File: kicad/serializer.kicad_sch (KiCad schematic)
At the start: 8 parts, among them U501 74HC165D, U502 74HC165D, U503 74HC165D, U504 74HC165D

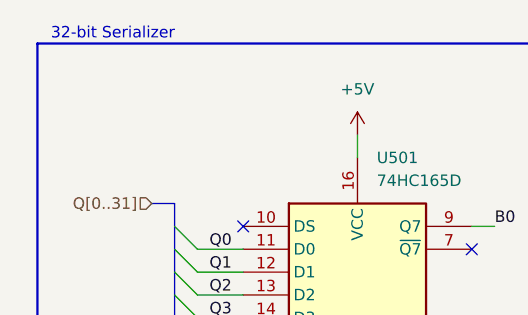
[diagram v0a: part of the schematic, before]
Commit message: rework isp header, update pinout
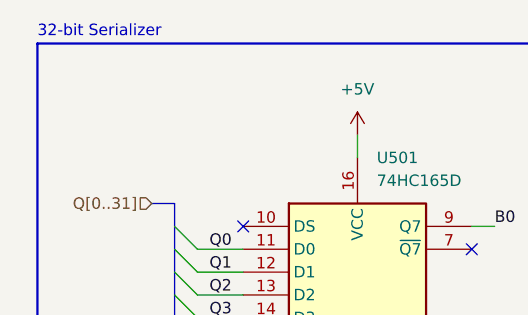
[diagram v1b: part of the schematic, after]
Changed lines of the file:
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@@
 	(title_block
 		(title "Frequency Counter")
-		(date "2025-11-19")
-		(rev "1.0")
+		(date "2025-12-25")
+		(rev "2.0-draft")
 		(company "vladaviedov.org")
 		(comment 1 "Maximum Precision (125 mHz ~ 325 MHz): 62.5 mHz")
@@
 	(text "32-bit Serializer"
 		(exclude_from_sim no)
-		(at 23.622 15.494 0)
+		(at 15.24 15.24 0)
 		(effects
 			(font
 				(size 1.27 1.27)
 			)
+			(justify left)
 		)
 	)

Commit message: replace alum caps with ceramics, change mpn labeling
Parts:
- CD501, CD502, CD503, CD504: MPN (none) -> KGM05AR51C104KH; Supplier https://www.digikey.com/en/products/detail/kyocera-avx/KGM0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 -> (none)
- U501, U502, U503, U504: MPN (none) -> 74HC165D,653; Supplier https://www.digikey.com/en/products/detail/nexperia-usa-inc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 -> (none)
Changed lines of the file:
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@@
 			)
 		)
-		(property "Supplier" "https://www.digikey.com/en/products/detail/kyocera-avx/KGM05AR51C104KH/563236"
+		(property "Supplier" ""
+			(at 66.04 66.04 0)
+			(effects
+				(font
+					(size 1.27 1.27)
+				)
+				(hide yes)
+			)
+		)
+		(property "MPN" "KGM05AR51C104KH"
 			(at 66.04 66.04 0)
 			(effects
@@
 			)
 		)
-		(property "Supplier" "https://www.digikey.com/en/products/detail/kyocera-avx/KGM05AR51C104KH/563236"
+		(property "Supplier" ""
+			(at 182.88 64.77 0)
+			(effects
+				(font
+					(size 1.27 1.27)
+				)
+				(hide yes)
+			)
+		)
+		(property "MPN" "KGM05AR51C104KH"
 			(at 182.88 64.77 0)
 			(effects
@@
 			)
 		)
-		(property "Supplier" "https://www.digikey.com/en/products/detail/kyocera-avx/KGM05AR51C104KH/563236"
+		(property "Supplier" ""
+			(at 124.46 66.04 0)
+			(effects
+				(font
+					(size 1.27 1.27)
+				)
+				(hide yes)
+			)
+		)
+		(property "MPN" "KGM05AR51C104KH"
 			(at 124.46 66.04 0)
 			(effects
@@
 			)
 		)
-		(property "Supplier" "https://www.digikey.com/en/products/detail/nexperia-usa-inc/74HC165D-653/763013"
+		(property "Supplier" ""
+			(at 50.8 52.07 0)
+			(effects
+				(font
+					(size 1.27 1.27)
+				)
+				(hide yes)
+			)
+		)
+		(property "MPN" "74HC165D,653"
 			(at 50.8 52.07 0)
 			(effects
@@
 			)
 		)
-		(property "Supplier" "https://www.digikey.com/en/products/detail/nexperia-usa-inc/74HC165D-653/763013"
+		(property "Supplier" ""
+			(at 167.64 52.07 0)
+			(effects
+				(font
+					(size 1.27 1.27)
+				)
+				(hide yes)
+			)
+		)
+		(property "MPN" "74HC165D,653"
 			(at 167.64 52.07 0)
 			(effects
@@
 			)
 		)
-		(property "Supplier" "https://www.digikey.com/en/products/detail/kyocera-avx/KGM05AR51C104KH/563236"
+		(property "Supplier" ""
+			(at 241.3 64.77 0)
+			(effects
+				(font
+					(size 1.27 1.27)
+				)
+				(hide yes)
+			)
+		)
+		(property "MPN" "KGM05AR51C104KH"
 			(at 241.3 64.77 0)
 			(effects
@@
 			)
 		)
-		(property "Supplier" "https://www.digikey.com/en/products/detail/nexperia-usa-inc/74HC165D-653/763013"
+		(property "Supplier" ""
+			(at 226.06 52.07 0)
+			(effects
+				(font
+					(size 1.27 1.27)
+				)
+				(hide yes)
+			)
+		)
+		(property "MPN" "74HC165D,653"
 			(at 226.06 52.07 0)
 			(effects
@@
 			)
 		)
-		(property "Supplier" "https://www.digikey.com/en/products/detail/nexperia-usa-inc/74HC165D-653/763013"
+		(property "Supplier" ""
 			(at 109.22 52.07 0)
 			(effects
+				(font
+					(size 1.27 1.27)
+				)
+				(hide yes)
+			)
+		)
+		(property "MPN" "74HC165D,653"
+			(at 109.22 52.07 0)
+			(effects

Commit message: assign references
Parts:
- renumbered CD501 to CD601, CD502 to CD602, CD503 to CD603, CD504 to CD604, U501 to U601, U502 to U602, U503 to U603, U504 to U604
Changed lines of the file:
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@@
 		(dnp no)
 		(fields_autoplaced yes)
-		(property "Reference" "CD501"
+		(property "Reference" "CD601"
 			(at 69.85 64.7699 0)
 			(effects
@@
 			(project ""
 				(path "/62339e8b-4e00-440f-8d81-4472a4f50c26/a3aa7686-14aa-4813-8b5a-e2293d297198"
-					(reference "CD501")
+					(reference "CD601")
 					(unit 1)
 				)
@@
 		(dnp no)
 		(fields_autoplaced yes)
-		(property "Reference" "#PWR0512"
+		(property "Reference" "#PWR0612"
 			(at 182.88 77.47 0)
 			(effects
@@
 			(project "frequency_counter"
 				(path "/62339e8b-4e00-440f-8d81-4472a4f50c26/a3aa7686-14aa-4813-8b5a-e2293d297198"
-					(reference "#PWR0512")
+					(reference "#PWR0612")
 					(unit 1)
 				)
@@
 		(dnp no)
 		(fields_autoplaced yes)
-		(property "Reference" "#PWR0515"
+		(property "Reference" "#PWR0615"
 			(at 241.3 62.23 0)
 			(effects
@@
 			(project "frequency_counter"
 				(path "/62339e8b-4e00-440f-8d81-4472a4f50c26/a3aa7686-14aa-4813-8b5a-e2293d297198"
-					(reference "#PWR0515")
+					(reference "#PWR0615")
 					(unit 1)
 				)
@@
 		(dnp no)
 		(fields_autoplaced yes)
-		(property "Reference" "CD503"
+		(property "Reference" "CD603"
 			(at 186.69 63.4999 0)
 			(effects
@@
 			(project "frequency_counter"
 				(path "/62339e8b-4e00-440f-8d81-4472a4f50c26/a3aa7686-14aa-4813-8b5a-e2293d297198"
-					(reference "CD503")
+					(reference "CD603")
 					(unit 1)
 				)
@@
 		(dnp no)
 		(fields_autoplaced yes)
-		(property "Reference" "#PWR0514"
+		(property "Reference" "#PWR0614"
 			(at 226.06 88.9 0)
 			(effects
@@
 			(project "frequency_counter"
 				(path "/62339e8b-4e00-440f-8d81-4472a4f50c26/a3aa7686-14aa-4813-8b5a-e2293d297198"
-					(reference "#PWR0514")
+					(reference "#PWR0614")
 					(unit 1)
 				)
@@
 		(dnp no)
 		(fields_autoplaced yes)
-		(property "Reference" "CD502"
+		(property "Reference" "CD602"
 			(at 128.27 64.7699 0)
 			(effects
@@
 			(project "frequency_counter"
 				(path "/62339e8b-4e00-440f-8d81-4472a4f50c26/a3aa7686-14aa-4813-8b5a-e2293d297198"
-					(reference "CD502")
+					(reference "CD602")
 					(unit 1)
 				)
@@
 		(dnp no)
 		(fields_autoplaced yes)
-		(property "Reference" "#PWR0503"
+		(property "Reference" "#PWR0603"
 			(at 66.04 63.5 0)
 			(effects
@@
 			(project "frequency_counter"
 				(path "/62339e8b-4e00-440f-8d81-4472a4f50c26/a3aa7686-14aa-4813-8b5a-e2293d297198"
-					(reference "#PWR0503")
+					(reference "#PWR0603")
 					(unit 1)
 				)
@@
 		(dnp no)
 		(fields_autoplaced yes)
-		(property "Reference" "#PWR0505"
+		(property "Reference" "#PWR0605"
 			(at 109.22 30.48 0)
 			(effects
@@
 			(project "frequency_counter"
 				(path "/62339e8b-4e00-440f-8d81-4472a4f50c26/a3aa7686-14aa-4813-8b5a-e2293d297198"
-					(reference "#PWR0505")
+					(reference "#PWR0605")
 					(unit 1)
 				)
@@
 		(dnp no)
 		(fields_autoplaced yes)
-		(property "Reference" "#PWR0502"
+		(property "Reference" "#PWR0602"
 			(at 50.8 88.9 0)
 			(effects
@@
 			(project ""
 				(path "/62339e8b-4e00-440f-8d81-4472a4f50c26/a3aa7686-14aa-4813-8b5a-e2293d297198"
-					(reference "#PWR0502")
+					(reference "#PWR0602")
 					(unit 1)
 				)
@@
 		(dnp no)
 		(fields_autoplaced yes)
-		(property "Reference" "#PWR0504"
+		(property "Reference" "#PWR0604"
 			(at 66.04 78.74 0)
 			(effects
@@
 			(project "frequency_counter"
 				(path "/62339e8b-4e00-440f-8d81-4472a4f50c26/a3aa7686-14aa-4813-8b5a-e2293d297198"
-					(reference "#PWR0504")
+					(reference "#PWR0604")
 					(unit 1)
 				)
@@
 		(dnp no)
 		(fields_autoplaced yes)
-		(property "Reference" "#PWR0513"
+		(property "Reference" "#PWR0613"
 			(at 226.06 30.48 0)
 			(effects
@@
 			(project "frequency_counter"
 				(path "/62339e8b-4e00-440f-8d81-4472a4f50c26/a3aa7686-14aa-4813-8b5a-e2293d297198"
-					(reference "#PWR0513")
+					(reference "#PWR0613")
 					(unit 1)
 				)
@@
 		(dnp no)
 		(fields_autoplaced yes)
-		(property "Reference" "U501"
+		(property "Reference" "U601"
 			(at 52.9433 29.21 0)
 			(effects
@@
 			(project "frequency_counter"
 				(path "/62339e8b-4e00-440f-8d81-4472a4f50c26/a3aa7686-14aa-4813-8b5a-e2293d297198"
-					(reference "U501")
+					(reference "U601")
 					(unit 1)
 				)
@@
 		(dnp no)
 		(fields_autoplaced yes)
-		(property "Reference" "#PWR0508"
+		(property "Reference" "#PWR0608"
 			(at 124.46 78.74 0)
 			(effects
@@
 			(project "frequency_counter"
 				(path "/62339e8b-4e00-440f-8d81-4472a4f50c26/a3aa7686-14aa-4813-8b5a-e2293d297198"
-					(reference "#PWR0508")
+					(reference "#PWR0608")
 					(unit 1)
 				)
@@
 		(dnp no)
 		(fields_autoplaced yes)
-		(property "Reference" "#PWR0507"
+		(property "Reference" "#PWR0607"
 			(at 124.46 63.5 0)
 			(effects
@@
 			(project "frequency_counter"
 				(path "/62339e8b-4e00-440f-8d81-4472a4f50c26/a3aa7686-14aa-4813-8b5a-e2293d297198"
-					(reference "#PWR0507")
+					(reference "#PWR0607")
 					(unit 1)
 				)
@@
 		(dnp no)
 		(fields_autoplaced yes)
-		(property "Reference" "#PWR0509"
+		(property "Reference" "#PWR0609"
 			(at 167.64 30.48 0)
 			(effects
@@
 			(project "frequency_counter"
 				(path "/62339e8b-4e00-440f-8d81-4472a4f50c26/a3aa7686-14aa-4813-8b5a-e2293d297198"
-					(reference "#PWR0509")
+					(reference "#PWR0609")
 					(unit 1)
 				)
@@
 		(dnp no)
 		(fields_autoplaced yes)
-		(property "Reference" "#PWR0511"
+		(property "Reference" "#PWR0611"
 			(at 182.88 62.23 0)
 			(effects
@@
 			(project "frequency_counter"
 				(path "/62339e8b-4e00-440f-8d81-4472a4f50c26/a3aa7686-14aa-4813-8b5a-e2293d297198"
-					(reference "#PWR0511")
+					(reference "#PWR0611")
 					(unit 1)
 				)
@@
 		(dnp no)
 		(fields_autoplaced yes)
-		(property "Reference" "U503"
+		(property "Reference" "U603"
 			(at 169.7833 29.21 0)
 			(effects
@@
 			(project "frequency_counter"
 				(path "/62339e8b-4e00-440f-8d81-4472a4f50c26/a3aa7686-14aa-4813-8b5a-e2293d297198"
-					(reference "U503")
+					(reference "U603")
 					(unit 1)
 				)
@@
 		(dnp no)
 		(fields_autoplaced yes)
-		(property "Reference" "CD504"
+		(property "Reference" "CD604"
 			(at 245.11 63.4999 0)
 			(effects
@@
 			(project "frequency_counter"
 				(path "/62339e8b-4e00-440f-8d81-4472a4f50c26/a3aa7686-14aa-4813-8b5a-e2293d297198"
-					(reference "CD504")
+					(reference "CD604")
 					(unit 1)
 				)
@@
 		(dnp no)
 		(fields_autoplaced yes)
-		(property "Reference" "U504"
+		(property "Reference" "U604"
 			(at 228.2033 29.21 0)
 			(effects
@@
 			(project "frequency_counter"
 				(path "/62339e8b-4e00-440f-8d81-4472a4f50c26/a3aa7686-14aa-4813-8b5a-e2293d297198"
-					(reference "U504")
+					(reference "U604")
 					(unit 1)
 				)
@@
 		(dnp no)
 		(fields_autoplaced yes)
-		(property "Reference" "#PWR0516"
+		(property "Reference" "#PWR0616"
 			(at 241.3 77.47 0)
 			(effects
@@
 			(project "frequency_counter"
 				(path "/62339e8b-4e00-440f-8d81-4472a4f50c26/a3aa7686-14aa-4813-8b5a-e2293d297198"
-					(reference "#PWR0516")
+					(reference "#PWR0616")
 					(unit 1)
 				)
@@
 		(dnp no)
 		(fields_autoplaced yes)
-		(property "Reference" "#PWR0510"
+		(property "Reference" "#PWR0610"
 			(at 167.64 88.9 0)
 			(effects
@@
 			(project "frequency_counter"
 				(path "/62339e8b-4e00-440f-8d81-4472a4f50c26/a3aa7686-14aa-4813-8b5a-e2293d297198"
-					(reference "#PWR0510")
+					(reference "#PWR0610")
 					(unit 1)
 				)
@@
 		(dnp no)
 		(fields_autoplaced yes)
-		(property "Reference" "#PWR0506"
+		(property "Reference" "#PWR0606"
 			(at 109.22 88.9 0)
 			(effects
@@
 			(project "frequency_counter"
 				(path "/62339e8b-4e00-440f-8d81-4472a4f50c26/a3aa7686-14aa-4813-8b5a-e2293d297198"
-					(reference "#PWR0506")
+					(reference "#PWR0606")
 					(unit 1)
 				)
@@
 		(dnp no)
 		(fields_autoplaced yes)
-		(property "Reference" "U502"
+		(property "Reference" "U602"
 			(at 111.3633 29.21 0)
 			(effects
@@
 			(project "frequency_counter"
 				(path "/62339e8b-4e00-440f-8d81-4472a4f50c26/a3aa7686-14aa-4813-8b5a-e2293d297198"
-					(reference "U502")
+					(reference "U602")
 					(unit 1)
 				)
@@
 		(dnp no)
 		(fields_autoplaced yes)
-		(property "Reference" "#PWR0501"
+		(property "Reference" "#PWR0601"
 			(at 50.8 30.48 0)
 			(effects
@@
 			(project ""
 				(path "/62339e8b-4e00-440f-8d81-4472a4f50c26/a3aa7686-14aa-4813-8b5a-e2293d297198"
-					(reference "#PWR0501")
-					(unit 1)
-				)
+					(reference "#PWR0601")
+					(unit 1)
+				)
